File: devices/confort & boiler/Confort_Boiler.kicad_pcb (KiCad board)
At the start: 2 copper layers, 61 x 78.1 mm, 25 parts, among them K1 DHT1, K2 DHT2, K3 DS18B20, P1 TOBOILER, Q1 BC558, U1 OPTO-TRANSISTOR4, U2 ARDUINO_MINI, U3 ENC28J60, U4 OPTO-TRANSISTOR4

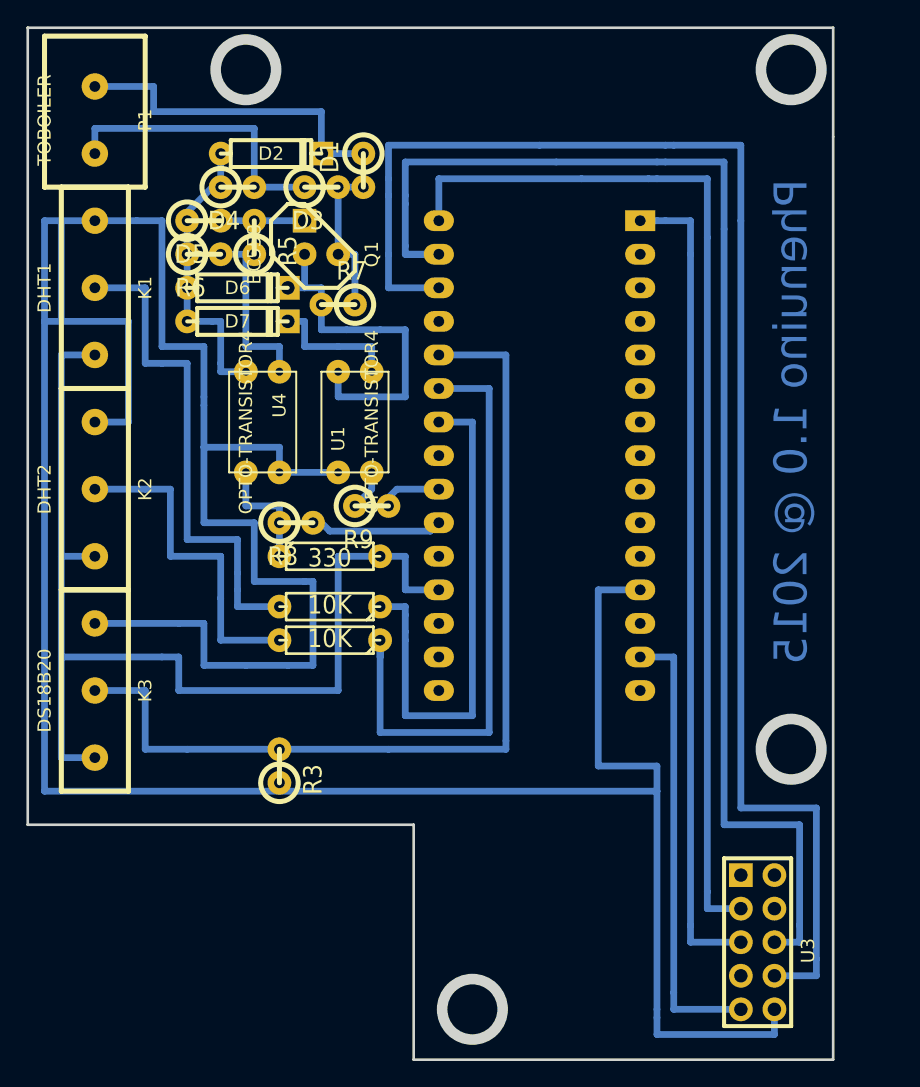
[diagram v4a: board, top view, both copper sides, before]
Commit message: added analog port as output for future use, changed dgs connectors to sil
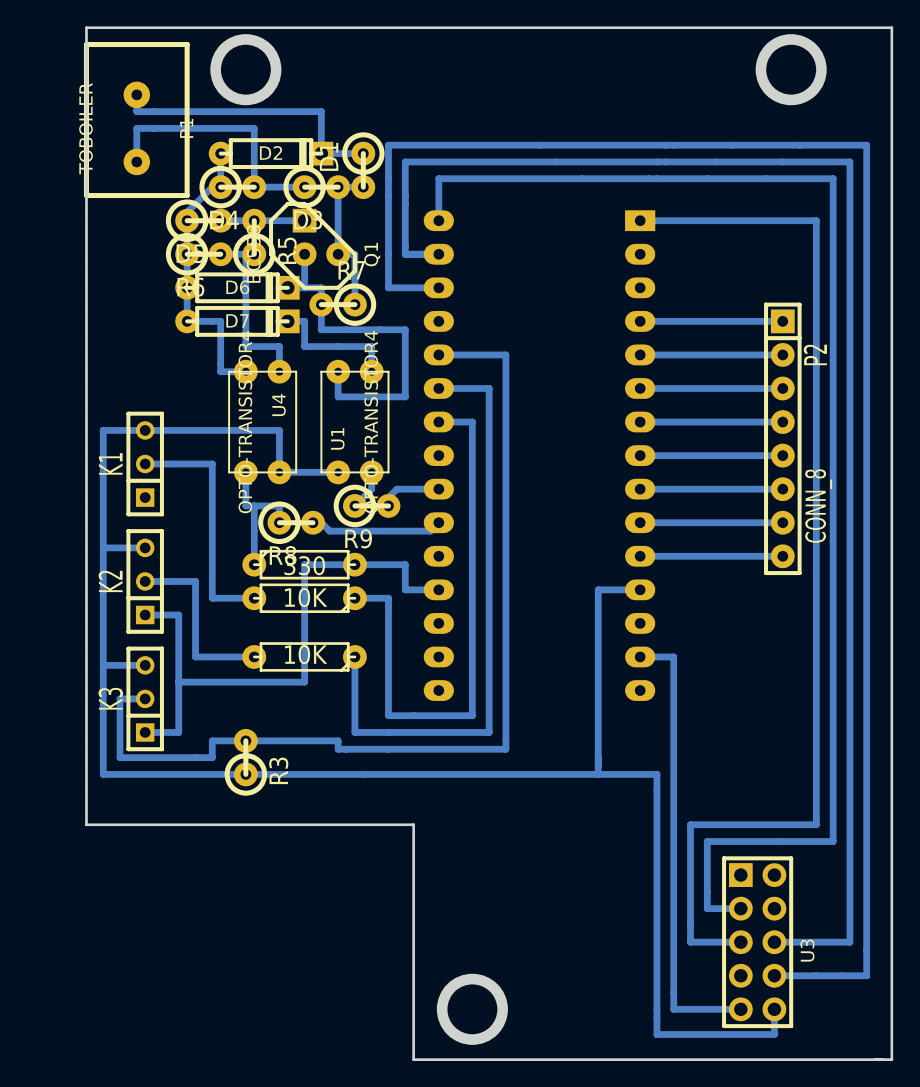
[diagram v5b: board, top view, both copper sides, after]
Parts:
- added P2: CONN_8, SIL-8, F.Cu at (83.8, 55.9)
- K1, K2, K3: footprint DG306-5.08-03 -> SIL-3
- moved K1 13.9 mm to (35.6, 57.8)
- moved K2 7.96 mm to (35.6, 66.7)
- moved K3 3.86 mm to (35.6, 75.6)
- moved P1 3.24 mm to (34.9, 32.4)
- moved R3 2.62 mm to (43.2, 80.0)
- moved R2 2.29 mm to (47.6, 72.4)
- moved R1 2.01 mm to (47.6, 67.9)
- moved R4 2.01 mm to (47.6, 65.4)
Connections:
- U2 pad 10: (no net) -> N-0000023
- U2 pad 11: (no net) -> N-0000024
- U2 pad 4: (no net) -> N-0000013
- U2 pad 5: (no net) -> N-0000018
- U2 pad 6: (no net) -> N-0000019
- U2 pad 7: (no net) -> N-0000020
- U2 pad 8: (no net) -> N-0000021
- U2 pad 9: (no net) -> N-0000022
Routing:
- net VCC: track 251.5 -> 143.5 mm
- net GND: track 116.2 -> 78.7 mm
- net N-000007: track 38.1 -> 18.4 mm
- net N-000004: track 62.2 -> 81.3 mm
- net N-000003: track 81.3 -> 100.3 mm
- net N-000009: track 25.4 -> 14.0 mm
- net N-0000024: track 0.00 -> 10.8 mm
- net N-0000023: track 0.00 -> 10.8 mm
- net N-0000022: track 0.00 -> 10.8 mm
- net N-0000021: track 0.00 -> 10.8 mm
- net N-0000020: track 0.00 -> 10.8 mm
- net N-0000019: track 0.00 -> 10.8 mm
- net N-0000018: track 0.00 -> 10.8 mm
- net N-0000013: track 0.00 -> 10.8 mm
- net N-000001: track 113.0 -> 120.6 mm
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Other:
- outline, holes or cut-outs redrawn
- board text removed: "Phenuino 1.0 @ 2015"
